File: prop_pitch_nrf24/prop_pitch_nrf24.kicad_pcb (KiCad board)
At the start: 2 copper layers, 62.5 x 22 mm, 53 parts, among them J1 LOAD1, J2 LOAD2, J3 AVR-UPDI-6, J4 SERVO2, J5 SERVO1, J6 SERIAL, Q1 MMSS8550, U1 ATtiny1616-M, U2 HX711, U3 TPS563208DDCR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

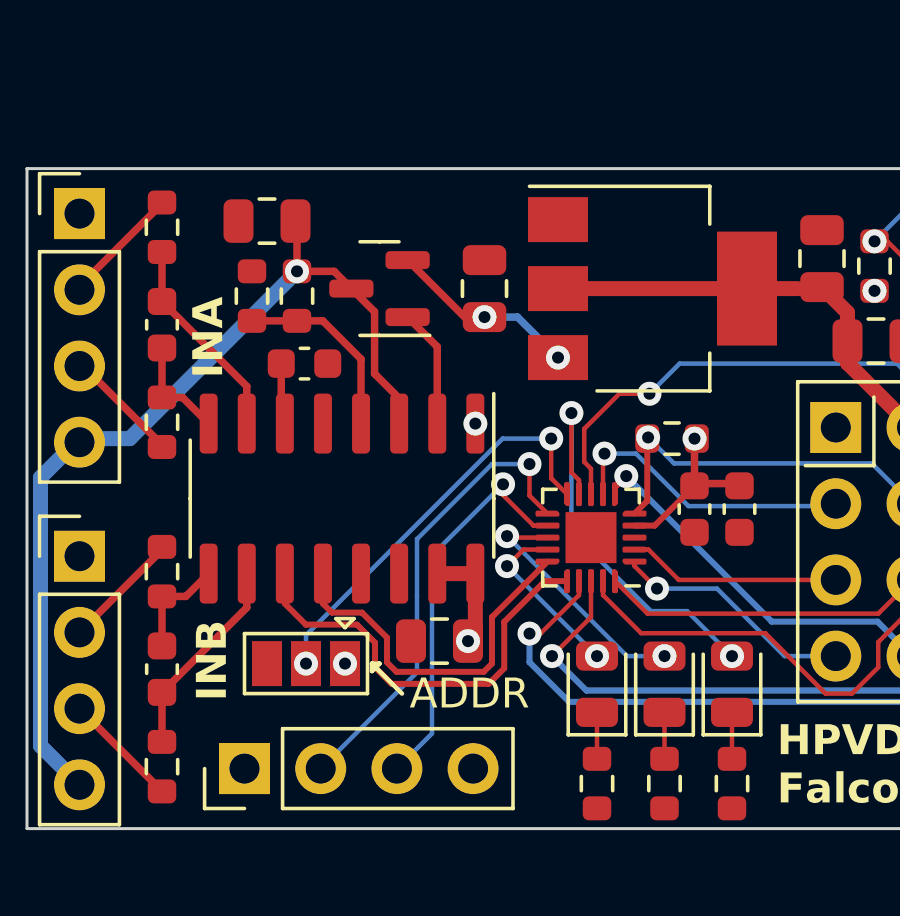
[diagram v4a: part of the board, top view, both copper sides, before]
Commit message: Cleaned up nRF schematic
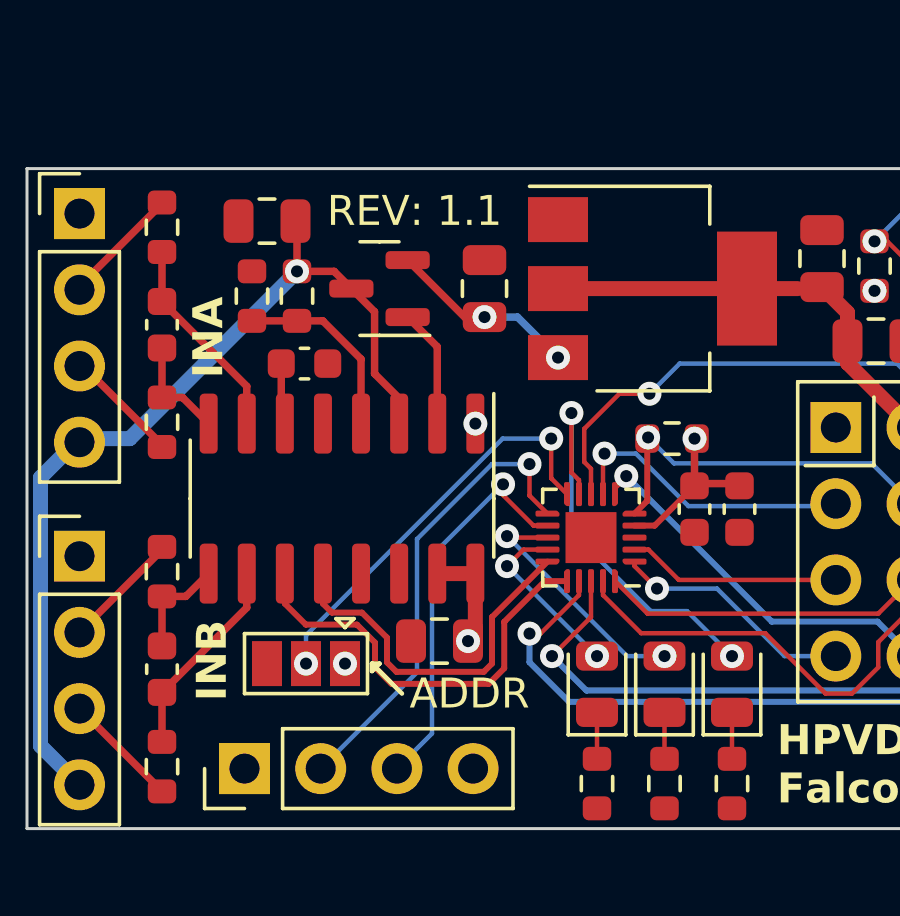
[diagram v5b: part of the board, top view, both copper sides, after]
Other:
- board text added: "REV: ${REVISION}"
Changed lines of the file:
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@@
     (title "Propellor Pitch and Monitor")
     (date "2023-12-08")
-    (rev "1.0")
+    (rev "1.1")
     (company "HPVDT")
   )
@@
     (effects (font (size 1 1) (thickness 0.2) bold) (justify left bottom))
   )
+  (gr_text "REV: ${REVISION}" (at 95 102.5) (layer "F.SilkS")
+    (effects (font (size 1 1) (thickness 0.15)) (justify left bottom))
+  )
   (gr_text "INB" (at 91.75 118.25 90) (layer "F.SilkS" knockout)
     (effects (font (size 1 1) (thickness 0.2) bold) (justify left bottom))
@@
   (segment (start 98 112.8495) (end 100.5 110.3495) (width 0.15) (layer "B.Cu") (net 43))
   (segment (start 100.5 110.3495) (end 101.75 110.3495) (width 0.15) (layer "B.Cu") (net 43))
-  (segment (start 98 114.75) (end 98 117.29) (width 0.15) (layer "B.Cu") (net 43))
-  (segment (start 98 114.75) (end 98 112.8495) (width 0.15) (layer "B.Cu") (net 43))
+  (segment (start 98 112.8495) (end 98 117.29) (width 0.15) (layer "B.Cu") (net 43))
   (segment (start 101.884552 112.4) (end 100.86833 111.383778) (width 0.15) (layer "F.Cu") (net 44))
   (segment (start 100.86833 111.383778) (end 100.86833 111.024) (width 0.15) (layer "F.Cu") (net 44))
@@
   (via (at 100.86833 111.024) (size 0.8) (drill 0.4) (layers "F.Cu" "B.Cu") (net 44))
   (segment (start 98.5 119.33) (end 97.33 120.5) (width 0.15) (layer "B.Cu") (net 44))
-  (segment (start 98.5 113.39233) (end 98.5 118) (width 0.15) (layer "B.Cu") (net 44))
-  (segment (start 98.5 118) (end 98.5 119.33) (width 0.15) (layer "B.Cu") (net 44))
+  (segment (start 98.5 113.39233) (end 98.5 119.33) (width 0.15) (layer "B.Cu") (net 44))
   (segment (start 100.86833 111.024) (end 98.5 113.39233) (width 0.15) (layer "B.Cu") (net 44))
   (segment (start 138.3875 114.6) (end 140.125 114.6) (width 0.2) (layer "F.Cu") (net 45))

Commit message: Touched up values for BOMs
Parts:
- C19, C20: value 22uF -> 22u
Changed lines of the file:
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@@
         (effects (font (size 1 1) (thickness 0.15)))
     )
-    (fp_text value "22uF" (at 0 1.68 -270) (layer "F.Fab")
+    (fp_text value "22u" (at 0 1.68 -270) (layer "F.Fab")
         (effects (font (size 1 1) (thickness 0.15)))
     )
@@
     (property "Sheetfile" "prop_pitch_nrf24.kicad_sch")
     (property "Sheetname" "")
+    (property "exclude_from_bom" "")
     (property "ki_description" "Solder Jumper, 3-pole, open")
     (property "ki_keywords" "Solder Jumper SPDT")
-    (attr exclude_from_pos_files)
+    (attr exclude_from_pos_files exclude_from_bom)
     (fp_text reference "JP1" (at 0 -1.8 180) (layer "F.SilkS") hide
         (effects (font (size 1 1) (thickness 0.15)))
@@
         (effects (font (size 1 1) (thickness 0.15)))
     )
-    (fp_text value "22uF" (at 1.25 -0.32 90) (layer "F.Fab")
-        (effects (font (size 1 1) (thickness 0.15)))
-    )
+    (fp_text value "22u" (at 1.25 -0.32 90) (layer "F.Fab")
+        (effects (font (size 1 1) (thickness 0.15)))
+    )
